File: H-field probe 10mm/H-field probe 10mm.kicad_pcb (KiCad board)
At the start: 4 copper layers, 74.8 x 24 mm, 1 part, among them J1 Conn_Coaxial

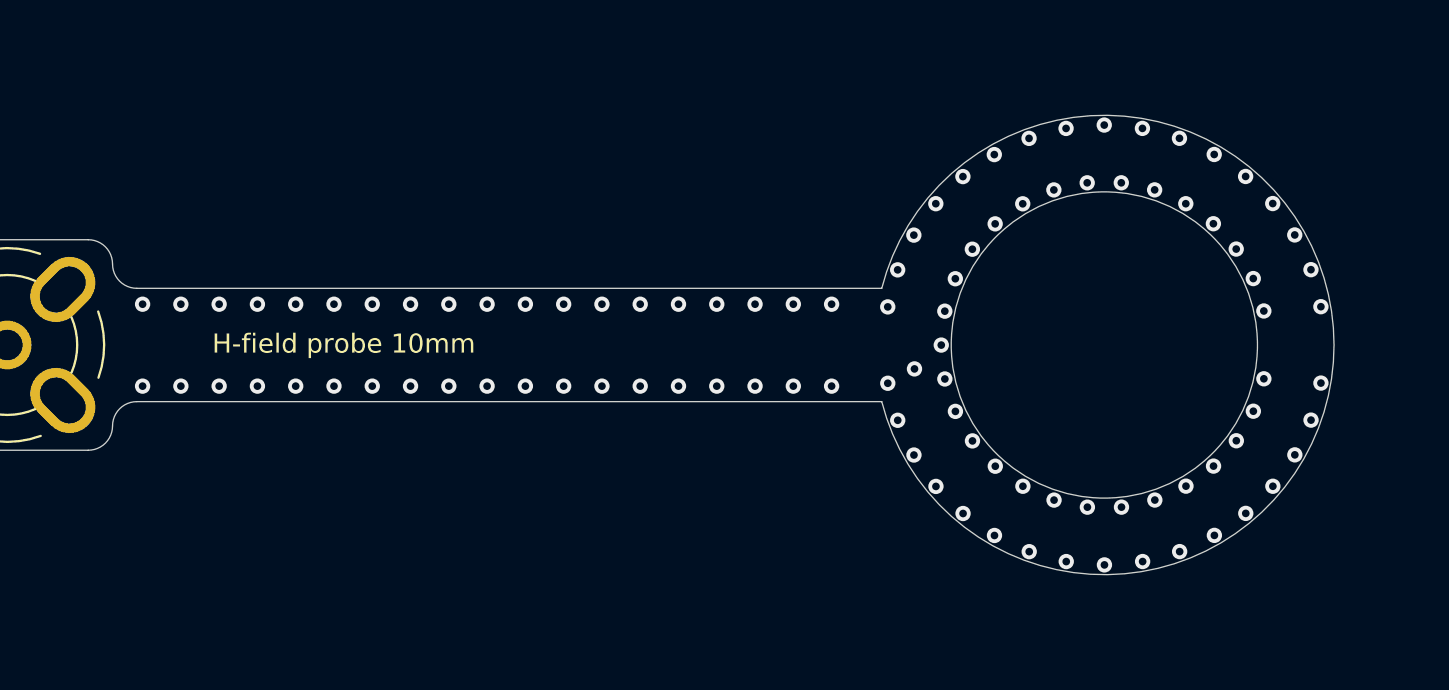
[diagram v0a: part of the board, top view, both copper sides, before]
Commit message: Fixed wrong diamter. Changed via size. Added text and logo
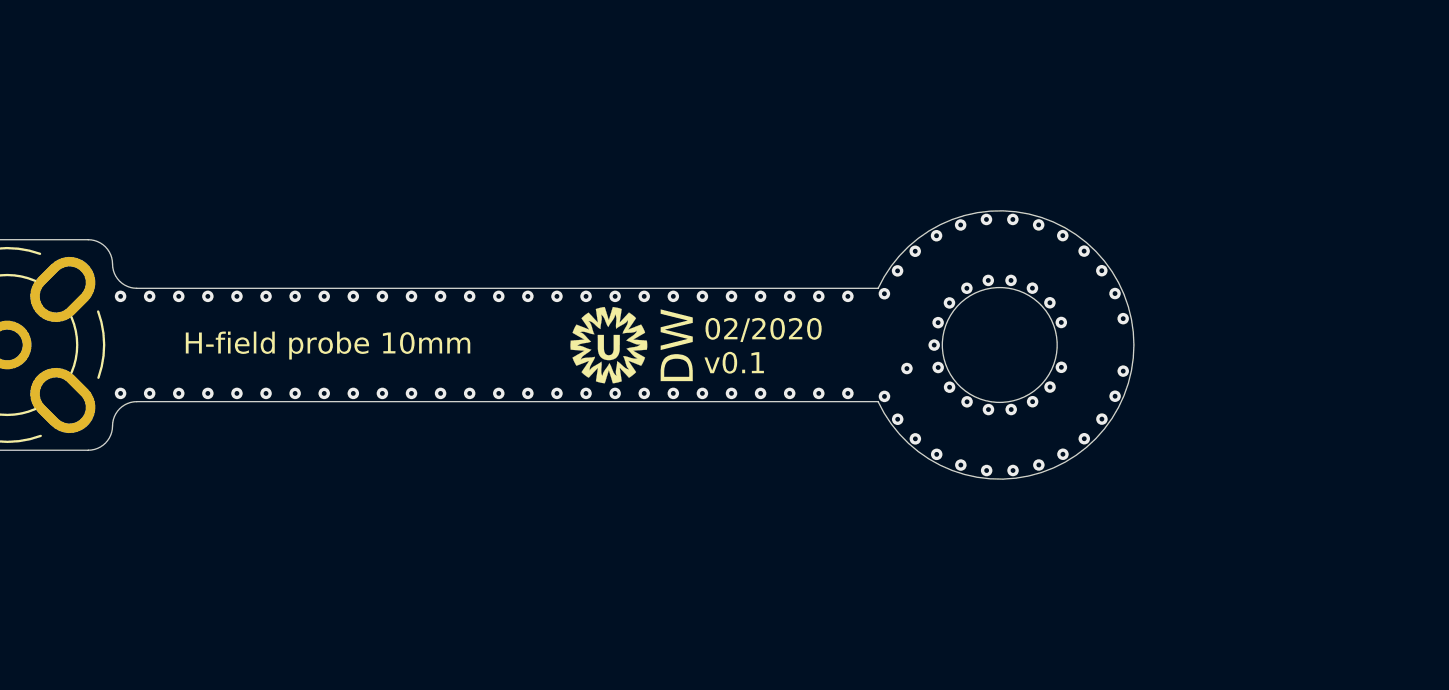
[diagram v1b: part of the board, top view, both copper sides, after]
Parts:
- added G***: LOGO, _Custom:UMC_logo_4mm, F.Cu at (142.3, 96.3)
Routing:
- net GND: vias 102 -> 96
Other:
- board size 74.8 x 24 mm -> 64.4 x 14 mm
- rule via_min_drill: 0.3 -> 0.25
- board text added: "02/2020 v0.1"
- board text added: "DW"

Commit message: Updated connector
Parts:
- turned J1 to 270 degrees
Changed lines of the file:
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@@
     (add_net "Net-(J1-Pad1)")
+  )
+  (module _Custom:BNC_SMA_Vertical (layer F.Cu)
+    (at 110.88 96.27 270)
+    (descr "BNC female PCB mount 4 pin straight chassis connector http://www.te.com/usa-en/product-1-1478204-0.html")
+    (tags "BNC female PCB mount 4 pin straight chassis connector ")
+    (fp_text reference J1 (at -4.32 0) (layer F.SilkS) hide
+      (effects (font (size 1 1) (thickness 0.15)))
+    )
+    (fp_text value Conn_Coaxial (at 0 6.5 90) (layer F.Fab)
+      (effects (font (size 1 1) (thickness 0.15)))
+    )
+    (fp_line (start -2.54 5.08) (end 2.54 5.08) (layer F.SilkS) (width 0.12))
+    (fp_text user %R (at 0 0 90) (layer F.Fab)
+      (effects (font (size 1 1) (thickness 0.15)))
+    )
+    (fp_line (start 5.5 -5.5) (end 5.5 5.5) (layer F.CrtYd) (width 0.05))
+    (fp_line (start 5.5 5.5) (end -5.5 5.5) (layer F.CrtYd) (width 0.05))
+    (fp_line (start -5.5 5.5) (end -5.5 -5.5) (layer F.CrtYd) (width 0.05))
+    (fp_line (start -5.5 -5.5) (end 5.5 -5.5) (layer F.CrtYd) (width 0.05))
+    (fp_circle (center 0 0) (end 4.8 0) (layer F.Fab) (width 0.1))
+    (fp_arc (start 0 0) (end -4.75 1.75) (angle 40) (layer F.SilkS) (width 0.12))
+    (fp_arc (start 0 0) (end 4.75 -1.75) (angle 40) (layer F.SilkS) (width 0.12))
+    (fp_arc (start 0 0) (end -1.75 -4.75) (angle 40) (layer F.SilkS) (width 0.12))
+    (fp_circle (center 0 0) (end 3.175 0) (layer F.Fab) (width 0.1))
+    (fp_arc (start 0 0) (end 3.355 -1.45) (angle 46.74710926) (layer F.SilkS) (width 0.12))
+    (fp_arc (start 0 0) (end -3.355 1.45) (angle 46.74710926) (layer F.SilkS) (width 0.12))
+    (fp_arc (start 0 0) (end -1.45 -3.355) (angle 46.74710926) (layer F.SilkS) (width 0.12))
+    (fp_arc (start 0 0) (end 1.45 3.355) (angle 46.74710926) (layer F.SilkS) (width 0.12))
+    (pad 2 thru_hole oval (at -2.9 -2.9 315) (size 2.7 3.7) (drill oval 1.7 2.7) (layers *.Cu *.Mask)
+      (net 1 GND))
+    (pad 1 thru_hole circle (at 0 0 270) (size 2.54 2.54) (drill 1.6) (layers *.Cu *.Mask)
+      (net 2 "Net-(J1-Pad1)"))
+    (pad 2 thru_hole oval (at 2.9 -2.9 225) (size 2.7 3.7) (drill oval 1.7 2.7) (layers *.Cu *.Mask)
+      (net 1 GND))
+    (pad 2 thru_hole oval (at -2.9 2.9 225) (size 2.7 3.7) (drill oval 1.7 2.7) (layers *.Cu *.Mask)
+      (net 1 GND))
+    (pad 2 thru_hole oval (at 2.9 2.9 315) (size 2.7 3.7) (drill oval 1.7 2.7) (layers *.Cu *.Mask)
+      (net 1 GND))
+    (model :_Custom_3D:BNC_73171-3356.stp
+      (offset (xyz 0 -22.7 6.1))
+      (scale (xyz 1 1 1))
+      (rotate (xyz -90 0 0))
+    )
   )
   (module _Custom:UMC_logo_4mm (layer F.Cu)
@@
       (xy 0.212034 -1.990841)) (layer F.SilkS) (width 0.01))
   )
-  (module _Custom:BNC_SMA_Vertical (layer F.Cu)
-    (at 110.88 96.27)
-    (descr "BNC female PCB mount 4 pin straight chassis connector http://www.te.com/usa-en/product-1-1478204-0.html")
-    (tags "BNC female PCB mount 4 pin straight chassis connector ")
-    (fp_text reference J1 (at -4.32 0 90) (layer F.SilkS) hide
-      (effects (font (size 1 1) (thickness 0.15)))
-    )
-    (fp_text value Conn_Coaxial (at 0 6.5) (layer F.Fab)
-      (effects (font (size 1 1) (thickness 0.15)))
-    )
-    (fp_arc (start 0 0) (end 1.45 3.355) (angle 46.74710926) (layer F.SilkS) (width 0.12))
-    (fp_arc (start 0 0) (end -1.45 -3.355) (angle 46.74710926) (layer F.SilkS) (width 0.12))
-    (fp_arc (start 0 0) (end -3.355 1.45) (angle 46.74710926) (layer F.SilkS) (width 0.12))
-    (fp_arc (start 0 0) (end 3.355 -1.45) (angle 46.74710926) (layer F.SilkS) (width 0.12))
-    (fp_circle (center 0 0) (end 3.175 0) (layer F.Fab) (width 0.1))
-    (fp_arc (start 0 0) (end -1.75 -4.75) (angle 40) (layer F.SilkS) (width 0.12))
-    (fp_arc (start 0 0) (end 4.75 -1.75) (angle 40) (layer F.SilkS) (width 0.12))
-    (fp_arc (start 0 0) (end 1.75 4.75) (angle 40) (layer F.SilkS) (width 0.12))
-    (fp_arc (start 0 0) (end -4.75 1.75) (angle 40) (layer F.SilkS) (width 0.12))
-    (fp_circle (center 0 0) (end 4.8 0) (layer F.Fab) (width 0.1))
-    (fp_line (start -5.5 -5.5) (end 5.5 -5.5) (layer F.CrtYd) (width 0.05))
-    (fp_line (start -5.5 5.5) (end -5.5 -5.5) (layer F.CrtYd) (width 0.05))
-    (fp_line (start 5.5 5.5) (end -5.5 5.5) (layer F.CrtYd) (width 0.05))
-    (fp_line (start 5.5 -5.5) (end 5.5 5.5) (layer F.CrtYd) (width 0.05))
-    (fp_text user %R (at 0 0) (layer F.Fab)
-      (effects (font (size 1 1) (thickness 0.15)))
-    )
-    (pad 2 thru_hole oval (at 2.9 2.9 45) (size 2.7 3.7) (drill oval 1.7 2.7) (layers *.Cu *.Mask)
-      (net 1 GND))
-    (pad 2 thru_hole oval (at -2.9 2.9 315) (size 2.7 3.7) (drill oval 1.7 2.7) (layers *.Cu *.Mask)
-      (net 1 GND))
-    (pad 2 thru_hole oval (at 2.9 -2.9 315) (size 2.7 3.7) (drill oval 1.7 2.7) (layers *.Cu *.Mask)
-      (net 1 GND))
-    (pad 1 thru_hole circle (at 0 0) (size 2.54 2.54) (drill 1.6) (layers *.Cu *.Mask)
-      (net 2 "Net-(J1-Pad1)") (clearance 0.2))
-    (pad 2 thru_hole oval (at -2.9 -2.9 45) (size 2.7 3.7) (drill oval 1.7 2.7) (layers *.Cu *.Mask)
-      (net 1 GND))
-    (model ${KISYS3DMOD}/Connector_Coaxial.3dshapes/BNC_TEConnectivity_1478204_Vertical.wrl
-      (at (xyz 0 0 0))
-      (scale (xyz 1 1 1))
-      (rotate (xyz 0 0 0))
-    )
-  )
   (gr_circle (center 162.735 96.27) (end 167.735 96.27) (layer Cmts.User) (width 0.01))
   (gr_circle (center 162.735 96.27) (end 165.735 96.27) (layer Edge.Cuts) (width 0.05))
@@
   (via (at 159.31 96.275) (size 0.6) (drill 0.25) (layers F.Cu B.Cu) (net 1))
   (via (at 157.885 97.5) (size 0.6) (drill 0.25) (layers F.Cu B.Cu) (net 1))
-  (segment (start 110.88 96.27) (end 157.73 96.275) (width 0.23495) (layer In1.Cu) (net 2))
   (via (at 156.712201 98.956996) (size 0.6) (drill 0.25) (layers F.Cu B.Cu) (net 1))
   (via (at 157.402472 100.150489) (size 0.6) (drill 0.25) (layers F.Cu B.Cu) (net 1))
@@
   (via (at 160.108084 94.072283) (size 0.6) (drill 0.25) (layers F.Cu B.Cu) (net 1))
   (via (at 159.514843 95.103279) (size 0.6) (drill 0.25) (layers F.Cu B.Cu) (net 1))
+  (segment (start 110.88 96.27) (end 157.73 96.275) (width 0.23495) (layer In1.Cu) (net 2))
   (zone (net 1) (net_name GND) (layer F.Cu) (hatch edge 0.508)
     (connect_pads (clearance 0))
